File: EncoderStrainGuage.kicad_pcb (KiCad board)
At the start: 2 copper layers, 116.8 x 116.8 mm, 34 parts, among them J1 Conn_01x05, J2 MM8130-2600RA2, J3 MM8130-2600RA2, Q1 NX3020NAK,215, U1 PIC16LF88-I_SO, U2 OPAMP, U3 CC2500RGP, U4 nRF51x22-QFxx, Y1 Crystal 26-27 MHZ

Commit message: Fixed everything
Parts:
- removed BT1: Battery_Cell, 1072TR:1072TR
- removed Q1: NX3020NAK,215, NX3020NAK_215:SOT95P230X110-3N
- added C10: 100nf, Capacitor_SMD:C_0603_1608Metric, F.Cu at (325.0, 84.2)
- added C11: 12p, Capacitor_SMD:C_0603_1608Metric, F.Cu at (333.3, 72.4)
- added C12: 12p, Capacitor_SMD:C_0603_1608Metric, F.Cu at (330.8, 74.1)
- added C13: 220pf, Capacitor_SMD:C_0603_1608Metric, F.Cu at (322.4, 84.5)
- added C14: 15p, Capacitor_SMD:C_0603_1608Metric, F.Cu at (330.8, 75.9)
- added C15: 15p, Capacitor_SMD:C_0603_1608Metric, F.Cu at (331.1, 77.6)
- added C16: 100nf, Capacitor_SMD:C_0603_1608Metric, F.Cu at (333.3, 74.1)
- added C17: 100nf, Capacitor_SMD:C_0603_1608Metric, F.Cu at (333.3, 75.9)
- added C18: 100nf, Capacitor_SMD:C_0603_1608Metric, F.Cu at (335.7, 72.4)
- added C19: 22pF, Capacitor_SMD:C_0603_1608Metric, F.Cu at (225.0, 105.0)
- added C20: 10uF, Capacitor_SMD:C_0603_1608Metric, F.Cu at (229.8, 100.3)
- added C8: 2.4 pf, Capacitor_SMD:C_0603_1608Metric, F.Cu at (330.8, 72.4)
- added IC1: LM60CIM3_NOPB, LM60CIM3_NOPB:SOT95P237X112-3N, F.Cu at (327.4, 81.0)
- added J4: Rotary Encoder, Connector_PinHeader_2.54mm:PinHeader_1x03_P2.54mm_Vertical, F.Cu at (311.0, 74.0)
- added J5: Conn_01x02_Male, Connector_PinHeader_2.54mm:PinHeader_1x02_P2.54mm_Vertical, F.Cu at (220.7, 101.4)
- added L3: 2.2uH, Inductor_SMD:L_0603_1608Metric_Pad1.05x0.95mm_HandSolder, F.Cu at (220.5, 107.5)
- added R10: 0, Resistor_SMD:R_0603_1608Metric, F.Cu at (335.7, 75.9)
- added R11: 100k, Resistor_SMD:R_0603_1608Metric, F.Cu at (331.1, 81.1)
- added R12: 0, Resistor_SMD:R_0603_1608Metric, F.Cu at (333.5, 79.4)
- added R13: 56k, Resistor_SMD:R_0603_1608Metric, F.Cu at (329.9, 84.2)
- added R14: 100k, Resistor_SMD:R_0603_1608Metric, F.Cu at (224.7, 107.5)
- added R15: 450k, Resistor_SMD:R_0603_1608Metric, F.Cu at (229.0, 105.0)
- added R8: 0, Resistor_SMD:R_0603_1608Metric, F.Cu at (327.4, 84.2)
- added R9: 100k, Resistor_SMD:R_0603_1608Metric, F.Cu at (333.5, 77.6)
- added VR1: StrainGuage, Connector_PinHeader_2.54mm:PinHeader_1x02_P2.54mm_Vertical, F.Cu at (327.3, 73.8)
- added Y2: Crystal, CM7V-T1A_32.768KHZ_12.5PF_20PP:CM7VT1A32768KHZ125PF20PPMTAQC, F.Cu at (320.5, 81.2)
- C1, C4: footprint Capacitor_SMD:C_0201_0603Metric -> Capacitor_SMD:C_0603_1608Metric
- C5: value 100nF -> 100n; footprint Capacitor_SMD:C_0201_0603Metric -> Capacitor_SMD:C_0603_1608Metric
- C6: value 15pF -> 1u; footprint Capacitor_SMD:C_0201_0603Metric -> Capacitor_SMD:C_0603_1608Metric
- C7: value 15pF -> 1m; footprint Capacitor_SMD:C_0201_0603Metric -> Capacitor_SMD:C_0603_1608Metric
- C9: value ? -> 1.5 pf
- L2: value ? -> 3.9 nH
- R1, R2, R5, R6: footprint Resistor_SMD:R_0201_0603Metric -> Resistor_SMD:R_0603_1608Metric
- R7: value 56 kohm -> 100k; footprint Resistor_SMD:R_0201_0603Metric -> Resistor_SMD:R_0603_1608Metric
- U3: value CC2500RGP -> CC2570RHAT; footprint CC2500RGP:QFN50P400X400X90-21N -> QFN40P500X500X90-41N:QFN40P500X500X90-41N
- U4: value nRF51x22-QFxx -> AP3428KTTR; footprint Package_DFN_QFN:QFN-48-1EP_6x6mm_P0.4mm_EP4.6x4.6mm -> Package_TO_SOT_SMD:SOT-23-5
- Y1: value Crystal 26-27 MHZ -> Crystal_GND24; footprint ECS-260-10-36B-CKY-TR:ECS240836QAESTR -> FA-128_32.0000MF20X-K3:FA128
- moved R1 258.5 mm to (319.2, 94.0)
- moved U4 194.5 mm to (225.4, 101.4)
- moved C5 152.0 mm to (335.7, 74.1), turned to 0 degrees
- moved R7 143.1 mm to (331.1, 79.4), turned to 0 degrees
- moved C7 137.8 mm to (320.0, 84.5)
- moved C6 137.6 mm to (317.5, 84.5)
- moved Y1 134.3 mm to (314.6, 82.7), turned to 0 degrees
- moved U3 1.41 mm to (188.0, 103.0)
- moved FL1 1.16 mm to (187.7, 107.9), turned to 270 degrees
- renumbered C8 to NP1, C11 to NP2, L3 to NP3, C10 to NP4
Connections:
- C3 pad 1: Net-(C3-Pad1) -> PSout
- C5 pad 1: Net-(C5-Pad1) -> +3V3
- C6 pad 1: Net-(C3-Pad1) -> Net-(C6-Pad1)
- C7 pad 1: Net-(C7-Pad1) -> GND
- C7 pad 2: GND -> +3V3
- FL1 pad 3: Net-(FL1-Pad3) -> RFpos
- FL1 pad 4: Net-(FL1-Pad4) -> RFneg
- L1 pad 1: Net-(C3-Pad1) -> PSout
- R1 pad 1: Net-(R1-Pad1) -> +3V3
- R1 pad 2: +3V3 -> Str1
- R4 pad 2: Net-(C3-Pad1) -> PSout
- R7 pad 1: GND -> Net-(R7-Pad1)
- R7 pad 2: Net-(R7-Pad2) -> GND
- U1 pad 1: Net-(U1-Pad1) -> PotOut
- U1 pad 11: Net-(U1-Pad11) -> UARTrx
- U1 pad 15: Net-(U1-Pad15) -> Reset
- U1 pad 16: Net-(U1-Pad16) -> Suspend
- U1 pad 18: Net-(U1-Pad18) -> Str1
- U1 pad 2: Net-(U1-Pad2) -> TempOut
- U1 pad 3: Net-(U1-Pad3) -> PSout
- U1 pad 6: Net-(U1-Pad6) -> RTS
- U1 pad 7: Net-(U1-Pad7) -> Sleep
- U1 pad 8: Net-(U1-Pad8) -> UARTtx
- U3 pad 1: Net-(U3-Pad1) -> GND
- U3 pad 10: Net-(C7-Pad1) -> +3V3
- U3 pad 11: Net-(BT1-Pad1) -> RTS
- U3 pad 12: Net-(FL1-Pad4) -> Net-(U3-Pad12)
- U3 pad 13: Net-(FL1-Pad3) -> GND
- U3 pad 14: Net-(BT1-Pad1) -> Net-(U3-Pad14)
- U3 pad 15: Net-(BT1-Pad1) -> Net-(U3-Pad15)
- U3 pad 16: GND -> Net-(U3-Pad16)
- U3 pad 17: Net-(R7-Pad2) -> GND
- U3 pad 18: Net-(BT1-Pad1) -> Sleep
- U3 pad 19: GND -> Suspend
- U3 pad 2: Net-(Q1-Pad1) -> GND
- U3 pad 20: Net-(U3-Pad20) -> Reset
- U3 pad 21: GND -> +3V3
- U3 pad 3: Net-(U3-Pad3) -> GND
- U3 pad 4: Net-(BT1-Pad1) -> GND
- U3 pad 5: Net-(C5-Pad1) -> UARTtx
- U3 pad 6: Net-(U3-Pad6) -> UARTrx
- U3 pad 8: Net-(C3-Pad1) -> Net-(R10-Pad2)
- U3 pad 9: Net-(BT1-Pad1) -> Net-(R7-Pad1)
- U4 pad 1: +3V3 -> Vin
- U4 pad 2: Net-(U4-Pad2) -> GND
- U4 pad 4: Net-(R1-Pad1) -> Vin
- U4 pad 5: GND -> +3V3
- Y1 pad 1: Net-(C3-Pad1) -> XOSC2
- Y1 pad 2: Net-(C7-Pad1) -> GND
- Y1 pad 3: (no net) -> XOSC1
- Y1 pad 4: (no net) -> GND
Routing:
- net Net-(C3-Pad1): track 13.8 -> 0.00 mm
- net Net-(Q1-Pad1): track 20.6 -> 7.51 mm
- net GND: track 8.20 -> 2.32 mm, vias 0 -> 44
- net Net-(FL1-Pad4): track 4.37 -> 0.00 mm
- net PSout: track 0.00 -> 4.18 mm
- net Net-(FL1-Pad1) (its old number): track 3.23 -> 0.00 mm
- net RFpos: track 0.00 -> 2.18 mm
- net RFneg: track 0.00 -> 1.97 mm
- net Net-(C5-Pad1): track 1.51 -> 0.00 mm
- net Net-(R7-Pad2): track 1.36 -> 0.00 mm
- net Net-(FL1-Pad1): track 6.51 -> 7.80 mm
- net MCLR: vias 40 -> 0
- added copper zone on B.Cu, net GND
- added copper zone on F.Cu, net GND
- removed copper zone on B.Cu, net (none)
- removed copper zone on F.Cu, net MCLR
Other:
- net class Default: clearance 0.2 -> 0.1
- rule trace_clearance: 0.2 -> 0.1

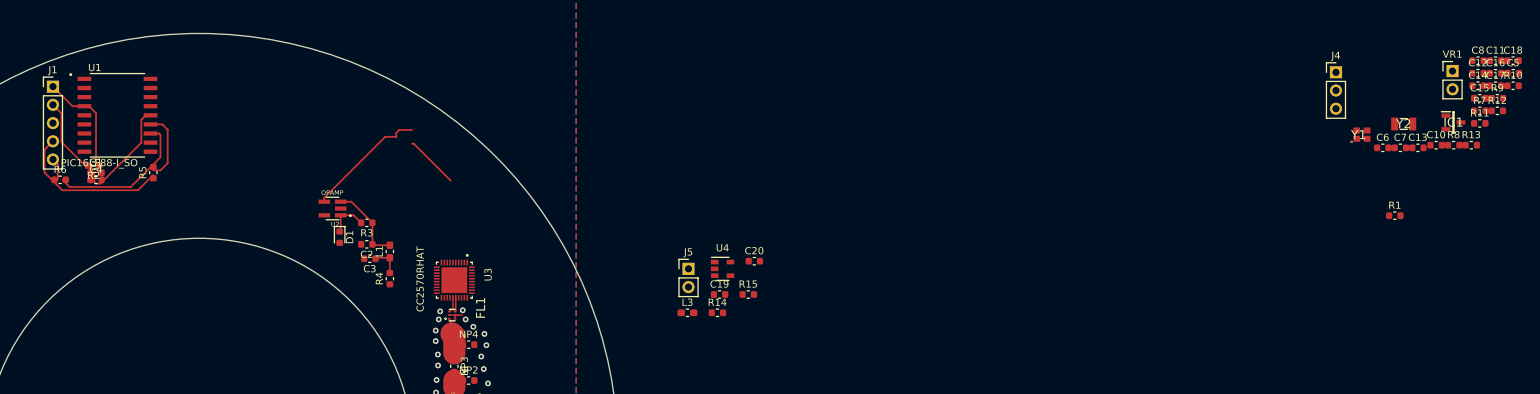
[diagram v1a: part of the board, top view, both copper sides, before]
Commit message: first route on the board
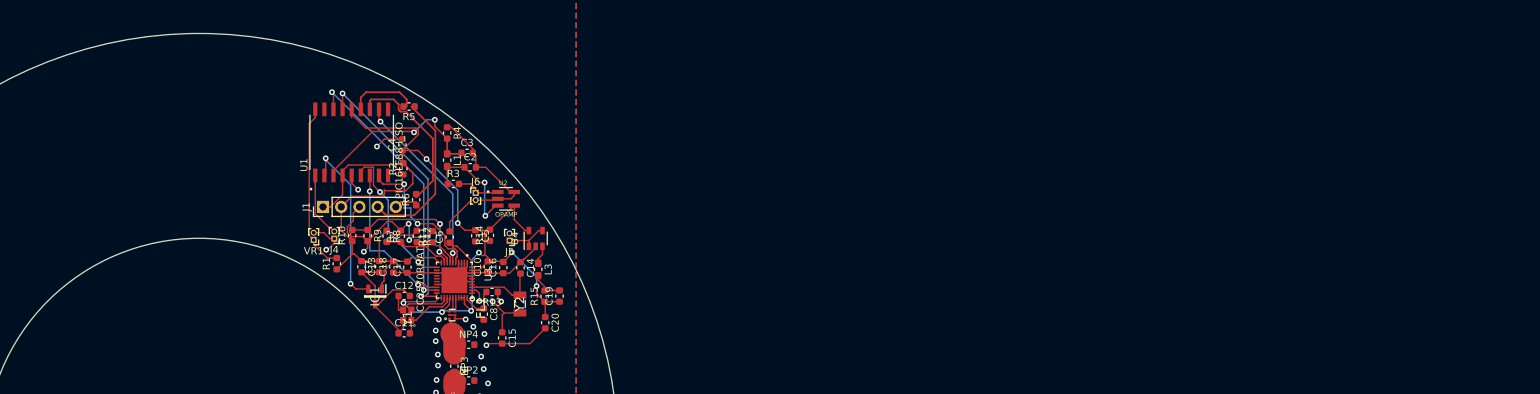
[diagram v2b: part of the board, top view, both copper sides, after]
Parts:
- removed C1: 100n, Capacitor_SMD:C_0603_1608Metric
- removed D1: D_Photo, Diode_SMD:D_0603_1608Metric
- added J6: Conn_01x02_Male, Connector_PinHeader_1.00mm:PinHeader_1x02_P1.00mm_Vertical, F.Cu at (191.0, 90.8)
- J4: footprint Connector_PinHeader_2.54mm:PinHeader_1x03_P2.54mm_Vertical -> Connector_PinHeader_1.00mm:PinHeader_1x02_P1.00mm_Vertical
- J5, VR1: footprint Connector_PinHeader_2.54mm:PinHeader_1x02_P2.54mm_Vertical -> Connector_PinHeader_1.00mm:PinHeader_1x02_P1.00mm_Vertical
- moved R10 163.3 mm to (173.8, 96.8), turned to 90 degrees
- moved VR1 160.6 mm to (168.4, 97.4), turned to 180 degrees
- moved C18 158.8 mm to (179.5, 101.2), turned to 90 degrees
- moved R9 158.8 mm to (175.9, 96.8), turned to 270 degrees
- moved C11 156.9 mm to (181.0, 110.4)
- moved C17 153.9 mm to (181.4, 101.2), turned to 90 degrees
- moved C12 153.0 mm to (181.0, 105.2)
- moved IC1 152.4 mm to (176.9, 105.3), turned to 270 degrees
- moved R12 151.8 mm to (182.8, 96.9), turned to 270 degrees
- moved R7 151.6 mm to (180.5, 96.9), turned to 90 degrees
- moved R8 149.4 mm to (178.6, 96.9), turned to 270 degrees
- moved C13 148.3 mm to (175.1, 101.1), turned to 270 degrees
- moved R1 147.8 mm to (171.6, 100.7), turned to 90 degrees
- moved R11 146.9 mm to (185.0, 96.9), turned to 90 degrees
- moved C5 146.6 mm to (190.9, 96.8), turned to 270 degrees
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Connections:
- U2 pad 4: +5V -> +3V3
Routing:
- net GND: track 2.32 -> 140.3 mm, vias 44 -> 49
- net +3V3: track 27.4 -> 156.0 mm, vias 0 -> 9
- net Reset: track 0.00 -> 38.8 mm, vias 0 -> 2
- net Suspend: track 0.00 -> 37.2 mm, vias 0 -> 2
- net UARTrx: track 0.00 -> 25.7 mm, vias 0 -> 2
- net TempOut: track 0.00 -> 24.2 mm, vias 0 -> 2
- net Str1: track 0.00 -> 23.5 mm
- net Sleep: track 0.00 -> 22.6 mm, vias 0 -> 2
- net RTS: track 0.00 -> 22.0 mm, vias 0 -> 2
- net PSout: track 4.18 -> 25.4 mm, vias 0 -> 2
- net UARTtx: track 0.00 -> 20.8 mm, vias 0 -> 2
- net Net-(R10-Pad2): track 0.00 -> 19.1 mm, vias 0 -> 2
- net +5V: track 17.0 -> 0.00 mm
- net XOSC32K1: track 0.00 -> 11.4 mm, vias 0 -> 2
- net XOSC32K2: track 0.00 -> 10.2 mm
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
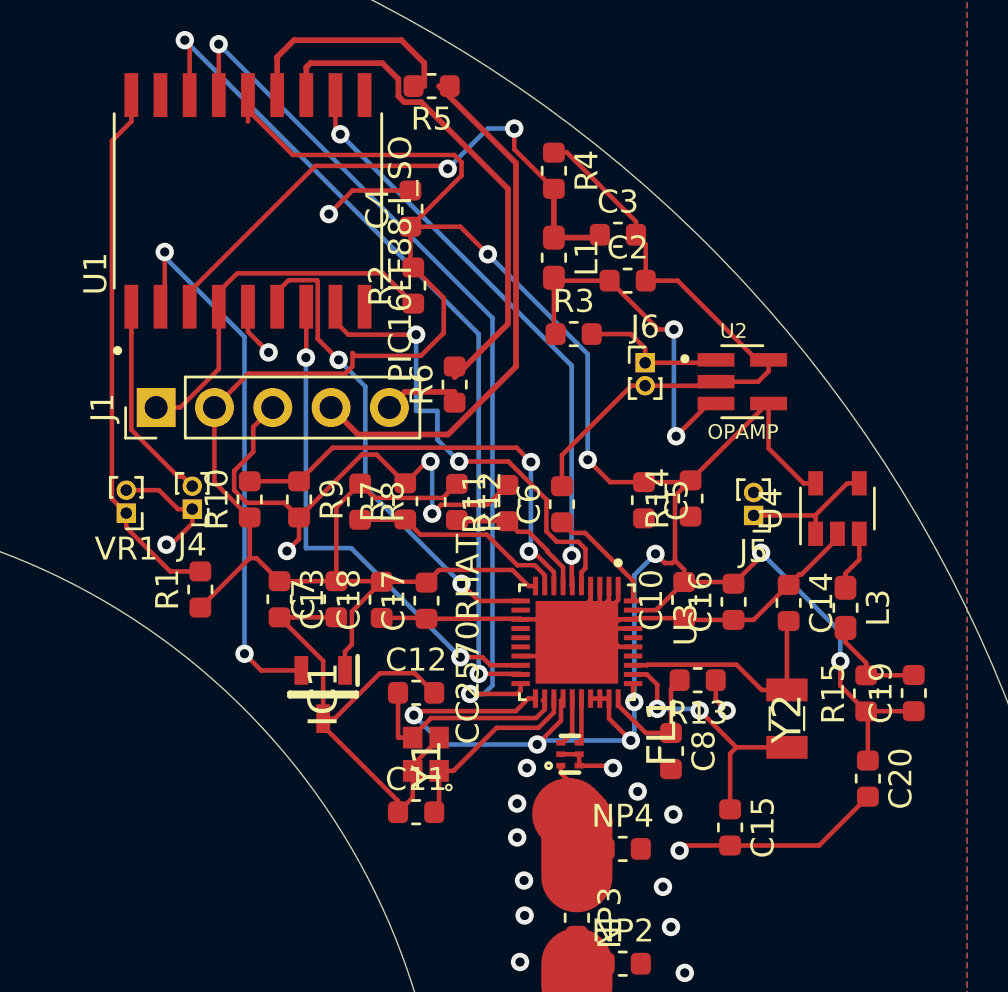
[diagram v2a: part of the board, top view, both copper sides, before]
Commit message: Fixed RF stuff and improved grounding. Still needs significant review
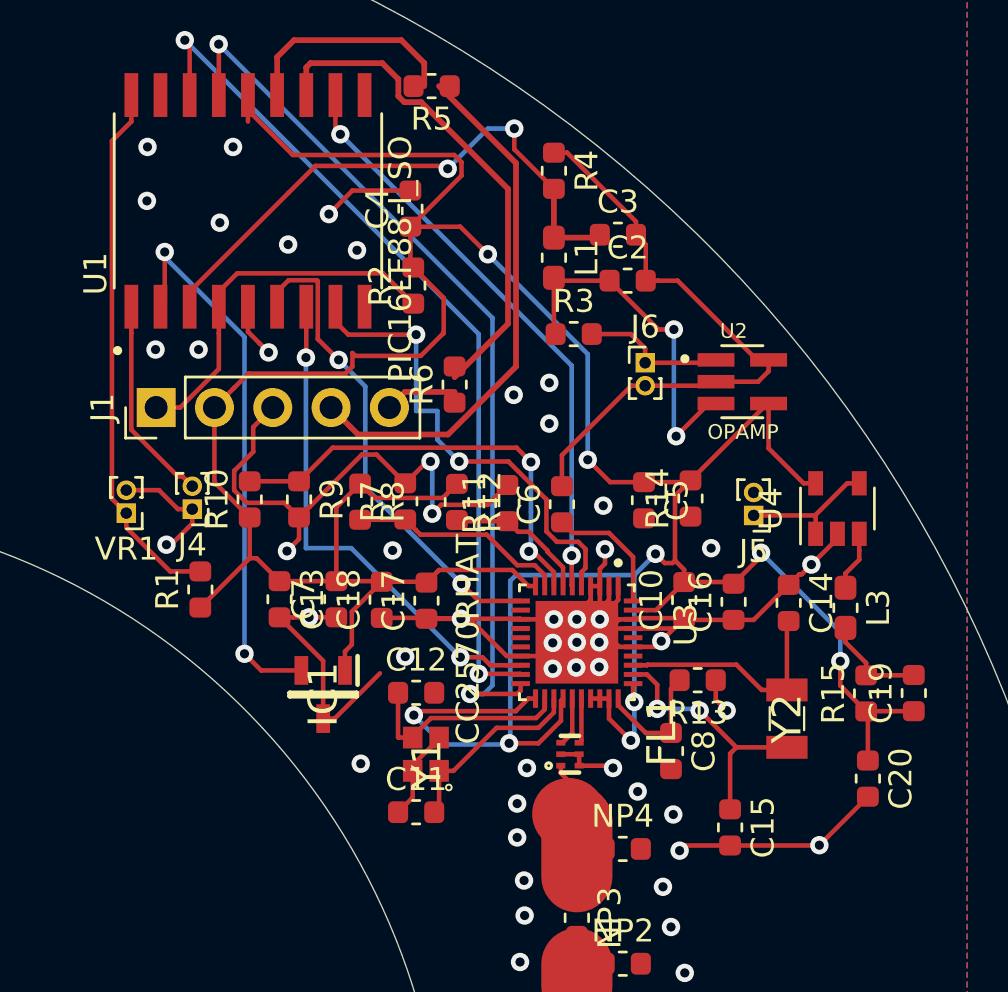
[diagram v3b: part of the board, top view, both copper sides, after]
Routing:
- net +3V3: track 156.0 -> 164.5 mm
- net GND: track 140.3 -> 144.5 mm, vias 49 -> 80
- net Net-(C6-Pad1): track 5.03 -> 5.64 mm

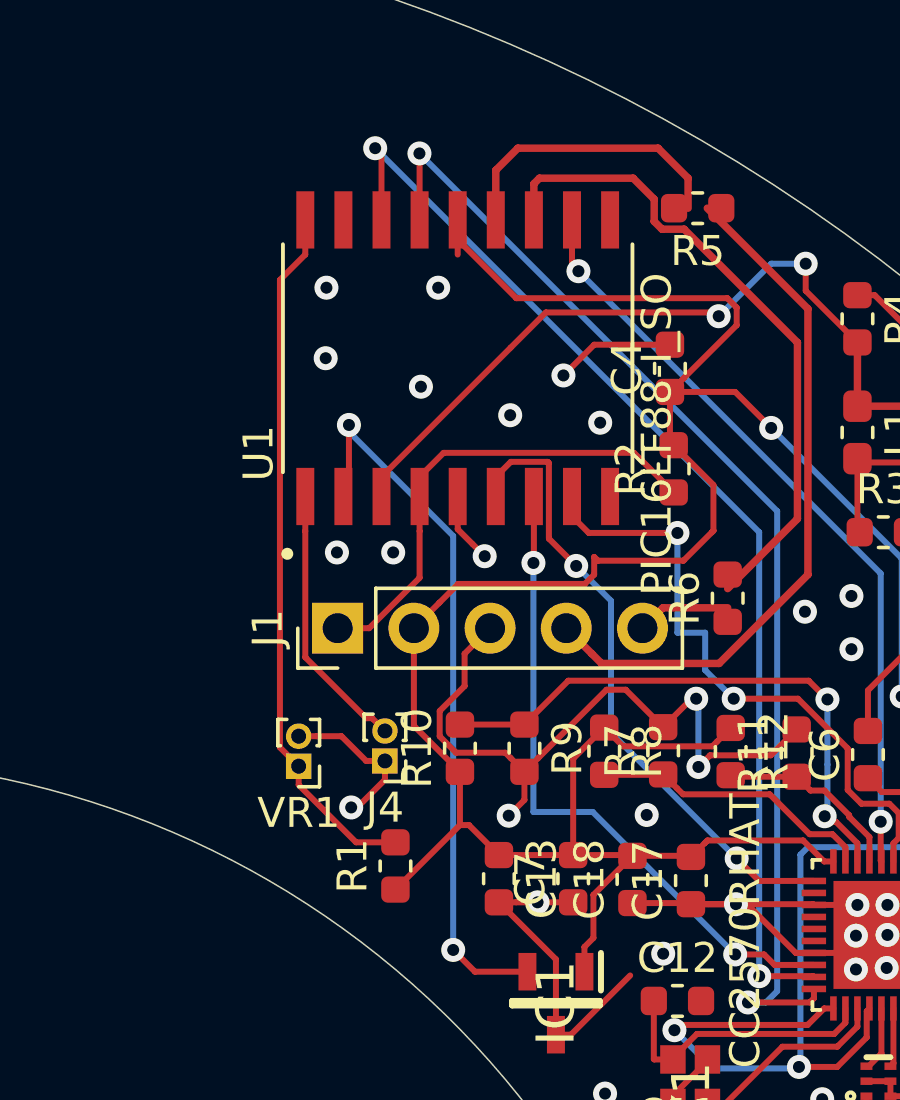
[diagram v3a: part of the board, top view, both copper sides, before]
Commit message: routed the wheatstone bridge to the rest of the board
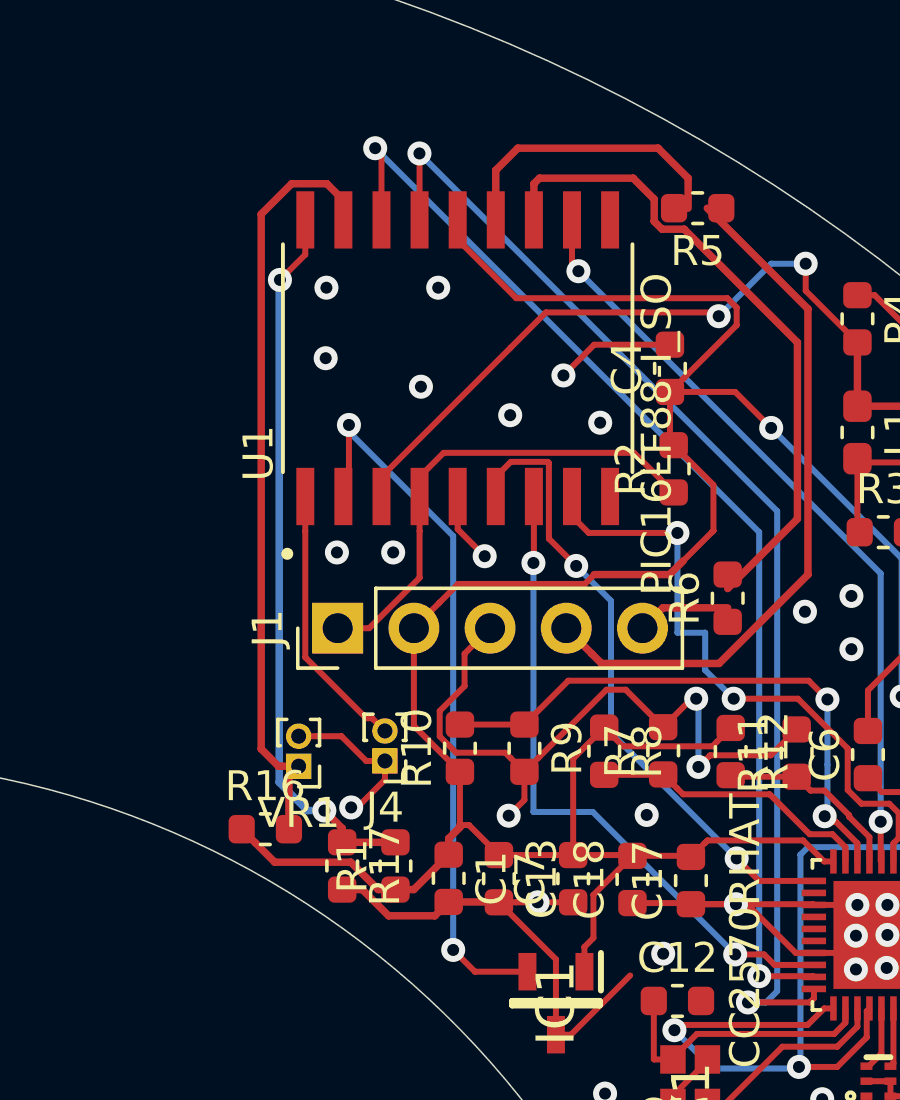
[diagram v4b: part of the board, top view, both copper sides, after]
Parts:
- added C1: 100n, Capacitor_SMD:C_0603_1608Metric, F.Cu at (173.4, 101.1)
- added R16: R, Resistor_SMD:R_0603_1608Metric, F.Cu at (167.3, 99.5)
- added R17: R, Resistor_SMD:R_0603_1608Metric, F.Cu at (169.8, 100.7)
- C2: value 310 pF -> 1nF
- C3: value 310 pF -> 2.2uF
- L1: value 1.58 uH -> 2.2uH
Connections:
- U1 pad 17: Net-(U1-Pad17) -> Str2
- VR1 pad 1: Str1 -> Str2
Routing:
- net Str2: track 0.00 -> 25.6 mm
- net GND: track 144.5 -> 150.3 mm
- net +3V3: track 164.5 -> 169.2 mm
- net Str1: track 23.5 -> 24.1 mm, vias 0 -> 2

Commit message: Redid the baord onto the correct one
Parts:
- moved J2 150.1 mm to (169.5, -24.0), turned to 90 degrees
- moved C9 147.4 mm to (167.5, -18.0), turned to 0 degrees
- moved L2 146.6 mm to (165.5, -13.9), turned to 90 degrees
- moved J3 145.7 mm to (173.5, -24.0), turned to 270 degrees
- moved AE1 141.3 mm to (165.5, -6.50), turned to 270 degrees
- moved NP1 141.3 mm to (167.5, -10.0), turned to 0 degrees
- moved NP2 139.6 mm to (177.5, -22.0), turned to 270 degrees
- moved NP3 139.3 mm to (179.5, -24.0), turned to 180 degrees
- moved C11 139.2 mm to (184.0, -28.8), turned to 90 degrees
- moved Y1 137.0 mm to (186.4, -29.0), turned to 270 degrees
- moved C12 134.2 mm to (189.4, -28.8)
- moved NP4 134.2 mm to (182.5, -22.0), turned to 270 degrees
- moved FL1 132.2 mm to (186.6, -24.3), turned to 180 degrees
- moved C15 130.8 mm to (188.5, -19.6)
- moved C8 128.3 mm to (186.3, -20.4)
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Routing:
- net GND: track 150.3 -> 98.8 mm, vias 80 -> 49
- net PGC: track 22.4 -> 2.42 mm
- net Str2: track 25.6 -> 7.10 mm
- net PSout: track 25.4 -> 7.42 mm, vias 2 -> 0
- net Str1: track 24.1 -> 6.28 mm, vias 2 -> 0
- net Suspend: track 37.2 -> 21.6 mm
- net UARTrx: track 25.7 -> 10.4 mm, vias 2 -> 0
- net Reset: track 38.8 -> 23.8 mm
- net Net-(R10-Pad2): track 19.1 -> 6.73 mm, vias 2 -> 0
- net TempOut: track 24.2 -> 11.9 mm
- net Net-(J1-Pad4): track 23.8 -> 13.5 mm
- net Net-(C2-Pad1): track 15.7 -> 5.90 mm, vias 2 -> 0
- net Net-(J1-Pad5): track 3.59 -> 12.7 mm
- net +3V3: track 169.2 -> 178.0 mm, vias 9 -> 14
- net PGD: track 10.9 -> 2.92 mm
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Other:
- board size 116.8 x 116.8 mm -> 90.6 x 37.4 mm
